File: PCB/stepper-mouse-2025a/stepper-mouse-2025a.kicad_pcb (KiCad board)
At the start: 2 copper layers, 85 x 114 mm, 95 parts, among them J1 STEPPER L, J2 STEPPER R, J3 Power, Q1 AO3401A, Q10 AO3402, Q11 BSS138, Q12 BSS138, Q13 BSS138, Q14 BSS138, Q2 AO3401A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

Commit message: Rev.1から使い勝手の悪いところを修正したもの
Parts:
- moved R2 79.3 mm to (173.5, 121.0)
- moved SW1 69.1 mm to (121.0, 129.0), turned to 180 degrees
- moved SW2 69.1 mm to (179.0, 129.0), turned to 180 degrees
- moved D6 67.1 mm to (124.0, 61.4), turned to -90 degrees
- moved D3 66.3 mm to (116.5, 61.4), turned to -90 degrees
- moved D8 66.3 mm to (181.0, 61.4), turned to -90 degrees
- moved D4 66.3 mm to (119.0, 61.4), turned to -90 degrees
- moved D5 66.2 mm to (121.5, 61.4), turned to -90 degrees
- moved D10 66.2 mm to (186.0, 61.4), turned to -90 degrees
- moved D7 66.2 mm to (178.5, 61.4), turned to -90 degrees
- moved D9 66.2 mm to (183.5, 61.4), turned to -90 degrees
- moved D1 62.5 mm to (122.3, 121.0), turned to 180 degrees
- moved D2 60.0 mm to (177.7, 121.0), turned to 0 degrees
- moved SW4 59.3 mm to (188.0, 127.0), turned to -90 degrees
- moved SW5 59.3 mm to (112.0, 127.0), turned to -90 degrees
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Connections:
- net /STP1AX renamed /STP1P1X
- net /STP1B renamed /STP1P2
- net /STP1DX renamed /STP1P4X
- net /STP2D renamed /STP2P4
- D1 pad 1: GND -> Net-(D1-K)
- D1 pad 2: Net-(D1-A) -> /LED1
- D10 pad 2: /STP2DX -> /STP2P4X
- D2 pad 1: GND -> Net-(D2-K)
- D2 pad 2: Net-(D2-A) -> /LED2
- D4 pad 2: /STP1BX -> /STP1P2X
- D5 pad 2: /STP1CX -> /STP1P3X
- D7 pad 2: /STP2AX -> /STP2P1X
- D8 pad 2: /STP2CX -> /STP2P2X
- D9 pad 2: /STP2BX -> /STP2P3X
- J1 pad 1: /STP1CX -> +5VP
- J1 pad 3: +5VP -> /STP1P2X
- J1 pad 4: /STP1BX -> /STP1P3X
- J2 pad 1: /STP2DX -> +5VP
- J2 pad 2: /STP2BX -> /STP2P1X
- J2 pad 3: +5VP -> /STP2P2X
- J2 pad 4: /STP2AX -> /STP2P3X
- J2 pad 5: /STP2CX -> /STP2P4X
- Q10 pad 3: /STP2DX -> /STP2P4X
- Q4 pad 3: /STP1BX -> /STP1P2X
- Q5 pad 3: /STP1CX -> /STP1P3X
- Q7 pad 3: /STP2AX -> /STP2P1X
- Q8 pad 3: /STP2BX -> /STP2P2X
- Q9 pad 3: /STP2CX -> /STP2P3X
- R1 pad 1: Net-(D1-A) -> GND
- R1 pad 2: /LED1 -> Net-(D1-K)
- R11 pad 2: /STP1D -> /STP1P4
- R13 pad 2: /STP2A -> /STP2P1
- R15 pad 2: /STP2B -> /STP2P2
- R17 pad 2: /STP2C -> /STP2P3
- R2 pad 1: /LED2 -> Net-(D2-K)
- R2 pad 2: Net-(D2-A) -> GND
- R5 pad 2: /STP1A -> /STP1P1
- R9 pad 2: /STP1C -> /STP1P3
- U1 pad 27: /STP1D -> /STP1P1
- U1 pad 29: /STP1A -> /STP1P3
- U1 pad 30: /STP1C -> /STP1P4
- U1 pad 7: /STP2C -> /STP2P1
- U1 pad 8: /STP2A -> /STP2P2
- U1 pad 9: /STP2B -> /STP2P3
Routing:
- net /LED2: track 2.98 -> 101.8 mm
- net /SW2: track 38.5 -> 117.6 mm
- net /STP1D: track 70.2 -> 0.00 mm, vias 1 -> 0
- net /STP1P1: track 0.00 -> 67.5 mm, vias 0 -> 1
- net /SW1: track 26.3 -> 86.5 mm
- net /STP2P3: track 0.00 -> 56.7 mm, vias 0 -> 1
- net /STP1A: track 55.8 -> 0.00 mm, vias 1 -> 0
- net /STP2B: track 55.4 -> 0.00 mm, vias 1 -> 0
- net /STP1P3: track 0.00 -> 53.1 mm, vias 0 -> 1
- net /STP2P2: track 0.00 -> 50.4 mm, vias 0 -> 1
- net /STP1C: track 49.2 -> 0.00 mm, vias 1 -> 0
- net /STP2A: track 49.1 -> 0.00 mm, vias 1 -> 0
- net /STP1P4: track 0.00 -> 46.2 mm, vias 0 -> 1
- net /LED1: track 12.1 -> 58.0 mm
- net /STP2P1: track 0.00 -> 43.4 mm, vias 0 -> 1
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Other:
- board text added: "P1"
- board text added: "P2"
- board text added: "P3"
- board text added: "P4"
- board text added: "POWER"
- board text added: "STEPPER MICRO MOUSE Rev. 2 @daisuke_ym 2025/07"
- board text removed: "A"
- board text removed: "B"
- board text removed: "G32"
- board text removed: "STEPPER MICRO MOUSE Rev. 1 @daisuke_ym 2025/07"
- board text removed: "~{A}"
- board text removed: "~{B}"

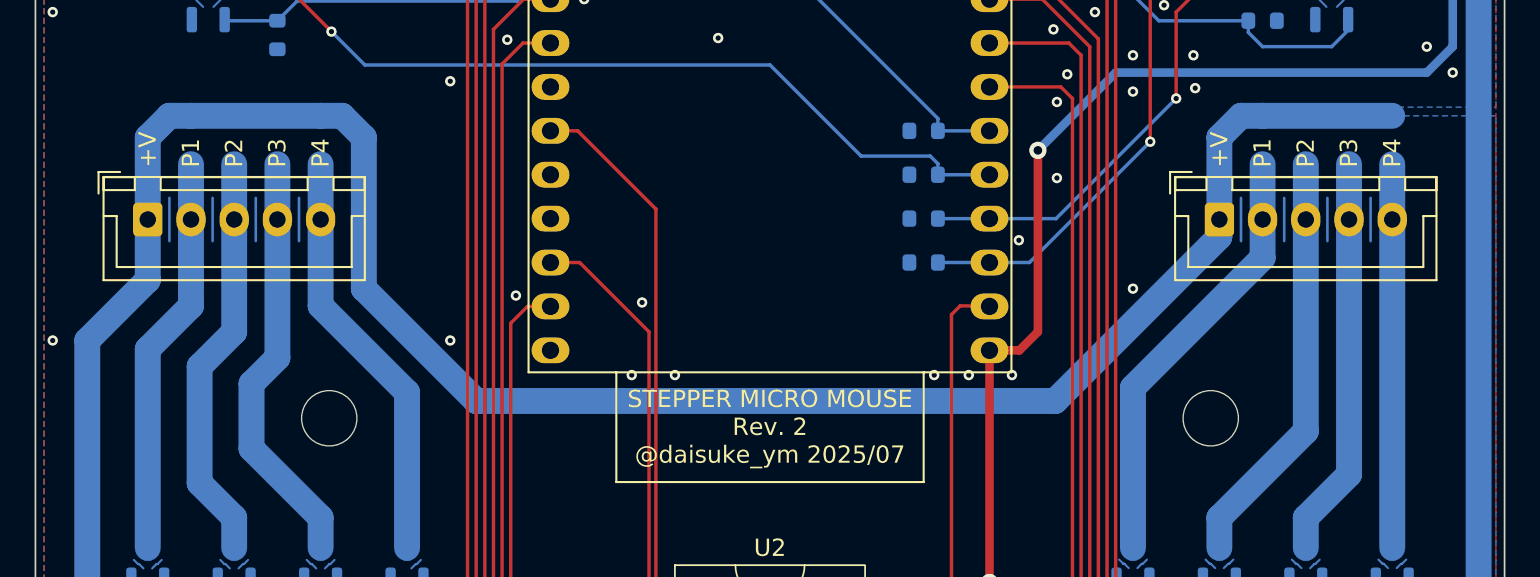
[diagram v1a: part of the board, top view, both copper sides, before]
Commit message: Rev.2のエラッタを修正
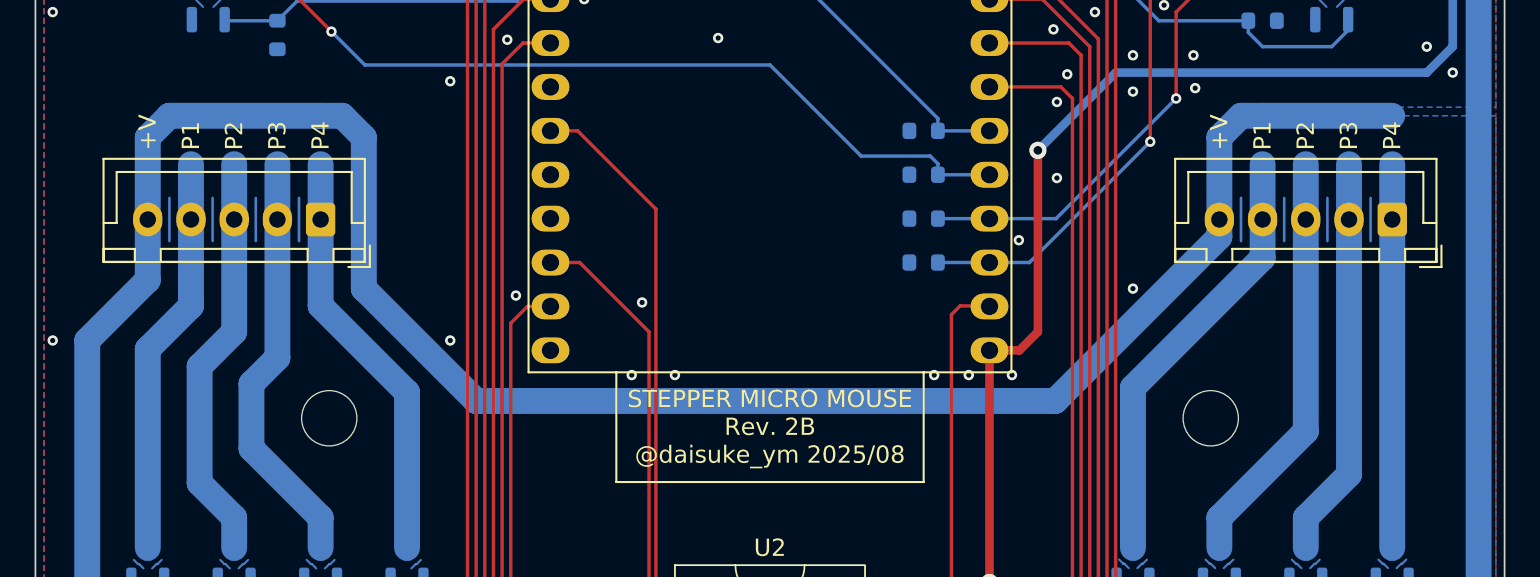
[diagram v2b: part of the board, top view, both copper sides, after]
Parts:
- moved J1 10.0 mm to (124.0, 66.0), turned to 180 degrees
- moved J2 10.0 mm to (186.0, 66.0), turned to 180 degrees
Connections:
- J1 pad 1: +5VP -> /STP1P4X
- J1 pad 2: /STP1P1X -> /STP1P3X
- J1 pad 4: /STP1P3X -> /STP1P1X
- J1 pad 5: /STP1P4X -> +5VP
- J2 pad 1: +5VP -> /STP2P4X
- J2 pad 2: /STP2P1X -> /STP2P3X
- J2 pad 4: /STP2P3X -> /STP2P1X
- J2 pad 5: /STP2P4X -> +5VP
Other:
- board text added: "G32"
- board text added: "STEPPER MICRO MOUSE Rev. 2B @daisuke_ym 2025/08"
- board text removed: "STEPPER MICRO MOUSE Rev. 2 @daisuke_ym 2025/07"
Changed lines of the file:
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@@
   (net 73 "Net-(D2-K)")
   (footprint "Connector_JST:JST_XH_B5B-XH-A_1x05_P2.50mm_Vertical" (layer "F.Cu")
-    (at 176 66)
+    (at 186 66 180)
     (descr "JST XH series connector, B5B-XH-A (http://www.jst-mfg.com/product/pdf/eng/eXH.pdf), generated with kicad-footprint-generator")
     (tags "connector JST XH vertical")
@@
     (fp_line (start 12.45 3.4) (end 12.45 -2.35)
       (stroke (width 0.1) (type solid)) (layer "F.Fab"))
-    (pad "1" thru_hole roundrect (at 0 0) (size 1.7 1.95) (drill 0.95) (layers "*.Cu" "*.Mask") (roundrect_rratio 0.1470588235)
-      (net 59 "+5VP") (pinfunction "Pin_1") (pintype "passive"))
-    (pad "2" thru_hole oval (at 2.5 0) (size 1.7 1.95) (drill 0.95) (layers "*.Cu" "*.Mask")
-      (net 15 "/STP2P1X") (pinfunction "Pin_2") (pintype "passive"))
-    (pad "3" thru_hole oval (at 5 0) (size 1.7 1.95) (drill 0.95) (layers "*.Cu" "*.Mask")
+    (pad "1" thru_hole roundrect (at 0 0 180) (size 1.7 1.95) (drill 0.95) (layers "*.Cu" "*.Mask") (roundrect_rratio 0.1470588235)
+      (net 33 "/STP2P4X") (pinfunction "Pin_1") (pintype "passive"))
+    (pad "2" thru_hole oval (at 2.5 0 180) (size 1.7 1.95) (drill 0.95) (layers "*.Cu" "*.Mask")
+      (net 17 "/STP2P3X") (pinfunction "Pin_2") (pintype "passive"))
+    (pad "3" thru_hole oval (at 5 0 180) (size 1.7 1.95) (drill 0.95) (layers "*.Cu" "*.Mask")
       (net 21 "/STP2P2X") (pinfunction "Pin_3") (pintype "passive"))
-    (pad "4" thru_hole oval (at 7.5 0) (size 1.7 1.95) (drill 0.95) (layers "*.Cu" "*.Mask")
-      (net 17 "/STP2P3X") (pinfunction "Pin_4") (pintype "passive"))
-    (pad "5" thru_hole oval (at 10 0) (size 1.7 1.95) (drill 0.95) (layers "*.Cu" "*.Mask")
-      (net 33 "/STP2P4X") (pinfunction "Pin_5") (pintype "passive"))
+    (pad "4" thru_hole oval (at 7.5 0 180) (size 1.7 1.95) (drill 0.95) (layers "*.Cu" "*.Mask")
+      (net 15 "/STP2P1X") (pinfunction "Pin_4") (pintype "passive"))
+    (pad "5" thru_hole oval (at 10 0 180) (size 1.7 1.95) (drill 0.95) (layers "*.Cu" "*.Mask")
+      (net 59 "+5VP") (pinfunction "Pin_5") (pintype "passive"))
     (model "${KICAD6_3DMODEL_DIR}/Connector_JST.3dshapes/JST_XH_B5B-XH-A_1x05_P2.50mm_Vertical.wrl"
       (offset (xyz 0 0 0))
@@
   )
   (footprint "Connector_JST:JST_XH_B5B-XH-A_1x05_P2.50mm_Vertical" (layer "F.Cu")
-    (at 114 66)
+    (at 124 66 180)
     (descr "JST XH series connector, B5B-XH-A (http://www.jst-mfg.com/product/pdf/eng/eXH.pdf), generated with kicad-footprint-generator")
     (tags "connector JST XH vertical")
@@
     (fp_line (start 12.45 3.4) (end 12.45 -2.35)
       (stroke (width 0.1) (type solid)) (layer "F.Fab"))
-    (pad "1" thru_hole roundrect (at 0 0) (size 1.7 1.95) (drill 0.95) (layers "*.Cu" "*.Mask") (roundrect_rratio 0.1470588235)
-      (net 59 "+5VP") (pinfunction "Pin_1") (pintype "passive"))
-    (pad "2" thru_hole oval (at 2.5 0) (size 1.7 1.95) (drill 0.95) (layers "*.Cu" "*.Mask")
-      (net 7 "/STP1P1X") (pinfunction "Pin_2") (pintype "passive"))
-    (pad "3" thru_hole oval (at 5 0) (size 1.7 1.95) (drill 0.95) (layers "*.Cu" "*.Mask")
+    (pad "1" thru_hole roundrect (at 0 0 180) (size 1.7 1.95) (drill 0.95) (layers "*.Cu" "*.Mask") (roundrect_rratio 0.1470588235)
+      (net 13 "/STP1P4X") (pinfunction "Pin_1") (pintype "passive"))
+    (pad "2" thru_hole oval (at 2.5 0 180) (size 1.7 1.95) (drill 0.95) (layers "*.Cu" "*.Mask")
+      (net 11 "/STP1P3X") (pinfunction "Pin_2") (pintype "passive"))
+    (pad "3" thru_hole oval (at 5 0 180) (size 1.7 1.95) (drill 0.95) (layers "*.Cu" "*.Mask")
       (net 10 "/STP1P2X") (pinfunction "Pin_3") (pintype "passive"))
-    (pad "4" thru_hole oval (at 7.5 0) (size 1.7 1.95) (drill 0.95) (layers "*.Cu" "*.Mask")
-      (net 11 "/STP1P3X") (pinfunction "Pin_4") (pintype "passive"))
-    (pad "5" thru_hole oval (at 10 0) (size 1.7 1.95) (drill 0.95) (layers "*.Cu" "*.Mask")
-      (net 13 "/STP1P4X") (pinfunction "Pin_5") (pintype "passive"))
+    (pad "4" thru_hole oval (at 7.5 0 180) (size 1.7 1.95) (drill 0.95) (layers "*.Cu" "*.Mask")
+      (net 7 "/STP1P1X") (pinfunction "Pin_4") (pintype "passive"))
+    (pad "5" thru_hole oval (at 10 0 180) (size 1.7 1.95) (drill 0.95) (layers "*.Cu" "*.Mask")
+      (net 59 "+5VP") (pinfunction "Pin_5") (pintype "passive"))
     (model "${KICAD6_3DMODEL_DIR}/Connector_JST.3dshapes/JST_XH_B5B-XH-A_1x05_P2.50mm_Vertical.wrl"
       (offset (xyz 0 0 0))
@@
     (effects (font (size 1 1) (thickness 0.15)) (justify left mirror))
   )
-  (gr_text "G33" (at 159.5 88) (layer "B.SilkS")
+  (gr_text "G32" (at 159.5 88) (layer "B.SilkS")
     (effects (font (size 1 1) (thickness 0.15)) (justify left mirror))
   )
@@
     (effects (font (size 1 1) (thickness 0.15)))
   )
-  (gr_text "P3" (at 183.5 63 90) (layer "F.SilkS")
+  (gr_text "P3" (at 183.5 62 90) (layer "F.SilkS")
     (effects (font (size 1 1) (thickness 0.15)) (justify left))
   )
-  (gr_text "P3" (at 121.5 63 90) (layer "F.SilkS")
+  (gr_text "P3" (at 121.5 62 90) (layer "F.SilkS")
     (effects (font (size 1 1) (thickness 0.15)) (justify left))
   )
-  (gr_text "P1" (at 178.5 63 90) (layer "F.SilkS")
+  (gr_text "P1" (at 178.5 62 90) (layer "F.SilkS")
     (effects (font (size 1 1) (thickness 0.15)) (justify left))
   )
@@
     (effects (font (size 1 1) (thickness 0.15)))
   )
-  (gr_text "P4" (at 124 63 90) (layer "F.SilkS")
+  (gr_text "P4" (at 124 62 90) (layer "F.SilkS")
     (effects (font (size 1 1) (thickness 0.15)) (justify left))
   )
@@
     (effects (font (size 1 1) (thickness 0.15)))
   )
-  (gr_text "P1" (at 116.5 63 90) (layer "F.SilkS")
+  (gr_text "P1" (at 116.5 62 90) (layer "F.SilkS")
     (effects (font (size 1 1) (thickness 0.15)) (justify left))
   )
-  (gr_text "P2" (at 181 63 90) (layer "F.SilkS")
+  (gr_text "P2" (at 181 62 90) (layer "F.SilkS")
     (effects (font (size 1 1) (thickness 0.15)) (justify left))
   )
-  (gr_text "+V" (at 114 63 90) (layer "F.SilkS")
+  (gr_text "+V" (at 114 62 90) (layer "F.SilkS")
     (effects (font (size 1 1) (thickness 0.15)) (justify left))
   )
-  (gr_text "P4" (at 186 63 90) (layer "F.SilkS")
+  (gr_text "P4" (at 186 62 90) (layer "F.SilkS")
     (effects (font (size 1 1) (thickness 0.15)) (justify left))
   )
-  (gr_text "STEPPER MICRO MOUSE\nRev. 2\n@daisuke_ym 2025/07" (at 150 78) (layer "F.SilkS")
+  (gr_text "STEPPER MICRO MOUSE\nRev. 2B\n@daisuke_ym 2025/08" (at 150 78) (layer "F.SilkS")
     (effects (font (size 1 1) (thickness 0.15)))
   )
@@
     (effects (font (size 1 1) (thickness 0.15)))
   )
-  (gr_text "+V" (at 176 63 90) (layer "F.SilkS")
+  (gr_text "+V" (at 176 62 90) (layer "F.SilkS")
     (effects (font (size 1 1) (thickness 0.15)) (justify left))
   )
@@
     (effects (font (size 1 1) (thickness 0.15)))
   )
-  (gr_text "P2" (at 119 63 90) (layer "F.SilkS")
+  (gr_text "P2" (at 119 62 90) (layer "F.SilkS")
     (effects (font (size 1 1) (thickness 0.15)) (justify left))
   )
